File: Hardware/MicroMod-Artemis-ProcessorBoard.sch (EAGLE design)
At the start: 36 parts, among them J1 MICROMOD-2222, U1 ARTEMIS_MODULESMD, U2 TSV524, U6 CH340E_MSOP10, Y1 32.768kHz

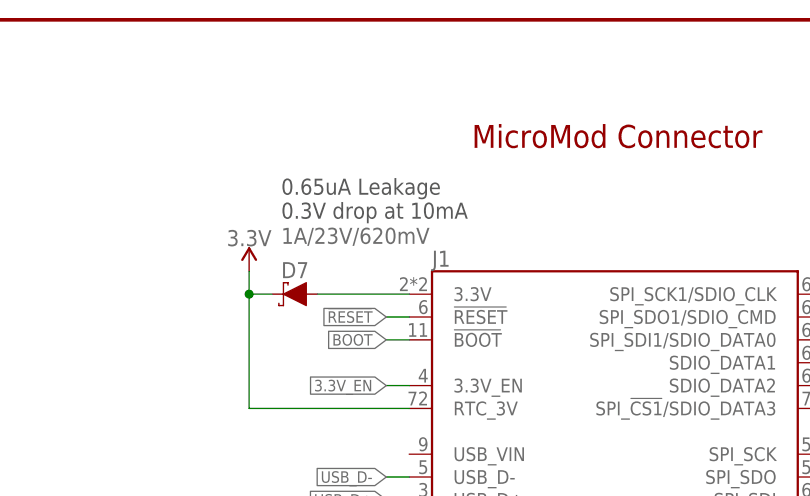
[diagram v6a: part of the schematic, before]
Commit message: Change 3.3V back feed diode to lower v-drop.
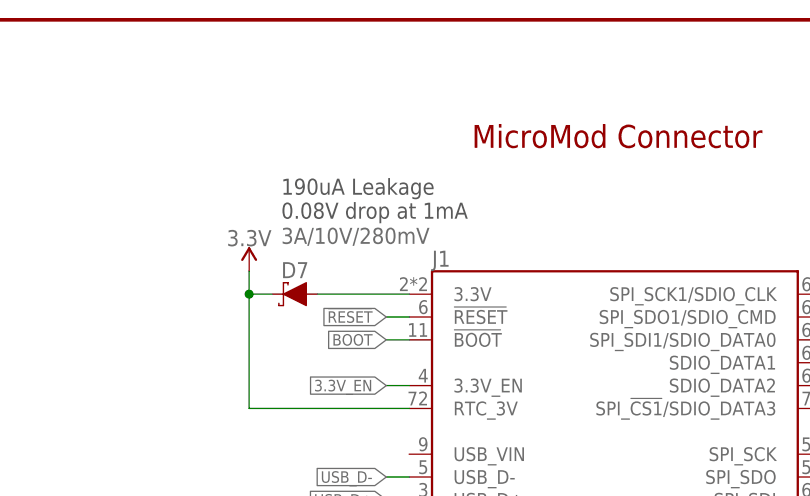
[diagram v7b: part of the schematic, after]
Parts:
- D7: value 1A/23V/620mV -> 3A/10V/280mV; device SparkFun-DiscreteSemi:DIODE-SCHOTTKY-BAT20J -> SparkFun-DiscreteSemi:DIODE-SCHOTTKY-BAT60A
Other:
- note added: "190uA Leakage 0.08V drop at 1mA"
- note removed: "0.65uA Leakage 0.3V drop at 10mA"
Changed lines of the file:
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@@
 <?xml version="1.0" encoding="utf-8"?>
 <!DOCTYPE eagle SYSTEM "eagle.dtd">
-<eagle version="9.6.0">
+<eagle version="9.6.2">
 <drawing>
 <settings>
@@
 <part name="GND8" library="SparkFun-PowerSymbols" deviceset="GND" device=""/>
 <part name="LOGO1" library="SparkFun-Aesthetics" deviceset="SFE_LOGO_NAME_FLAME" device=".1_INCH"/>
-<part name="D7" library="SparkFun-DiscreteSemi" deviceset="DIODE-SCHOTTKY" device="-BAT20J" value="1A/23V/620mV"/>
+<part name="D7" library="SparkFun-DiscreteSemi" deviceset="DIODE-SCHOTTKY" device="-BAT60A" value="3A/10V/280mV"/>
 <part name="SUPPLY1" library="SparkFun-PowerSymbols" deviceset="3.3V" device=""/>
 <part name="LOGO2" library="SparkFun-Aesthetics" deviceset="SFE_LOGO_FLAME" device=".1_INCH"/>
@@
 <text x="211.074" y="119.126" size="2.54" layer="94" font="vector" align="center">Status LED</text>
 <text x="211.074" y="144.526" size="2.54" layer="97" font="vector" align="center">Vin: 1.755 - 3.63V</text>
-<text x="176.276" y="257.302" size="1.778" layer="97">0.65uA Leakage
-0.3V drop at 10mA</text>
+<text x="176.276" y="257.302" size="1.778" layer="97">190uA Leakage
+0.08V drop at 1mA</text>
 <text x="342.9" y="243.84" size="1.27" layer="97" align="center">30uA (typ) per channel</text>
 </plain>

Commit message: Move CH340 to 3.3V side of diode. Replace D7 with 0.3uA leakage diode.
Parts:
- D7: value 3A/10V/280mV -> 1A/23V/620mV; device SparkFun-DiscreteSemi:DIODE-SCHOTTKY-BAT60A -> SparkFun-DiscreteSemi:DIODE-SCHOTTKY-BAT20J
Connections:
- removed net 3.3V_MAIN: D7.A, J1.3.3V
- new net V_BATT: C1.1, C3.1, C4.1, D7.C, J1.RTC_3V, R14.2, U1.VDD*2, U2G5.V+
- net 3.3V: now also D7.A, J1.3.3V; no longer C1.1, C3.1, C4.1, D7.C, J1.RTC_3V, R14.2, U1.VDD*2, U2G5.V+
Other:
- note added: "0.3uA Leakage 0.280V drop at 1mA"
- note added: "v1.7"
- note removed: "190uA Leakage 0.08V drop at 1mA"
- note removed: "v1.6"
- moved on the sheet: C2, C3, C4
